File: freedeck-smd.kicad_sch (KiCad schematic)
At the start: 27 parts, among them T1 TP-SM-C-100, T2 TP-SM-C-100, U1 RP2040, U2 W25Q128JV, Y1 ABM8-12.000MHZ-B2-T

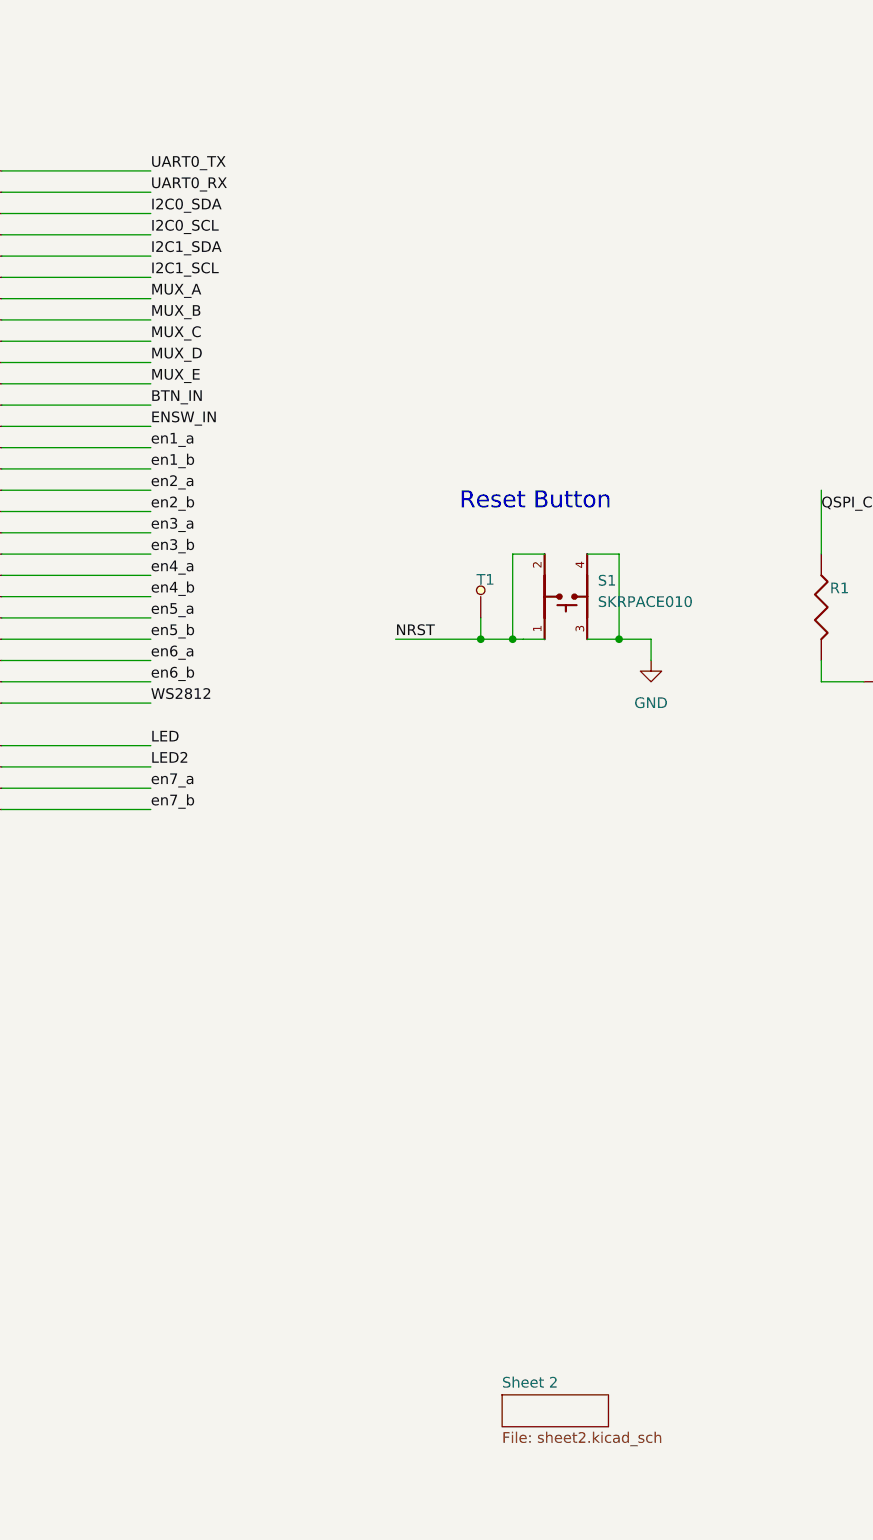
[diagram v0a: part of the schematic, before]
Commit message: Added multiplexers, changed i2c to spi, added external pins
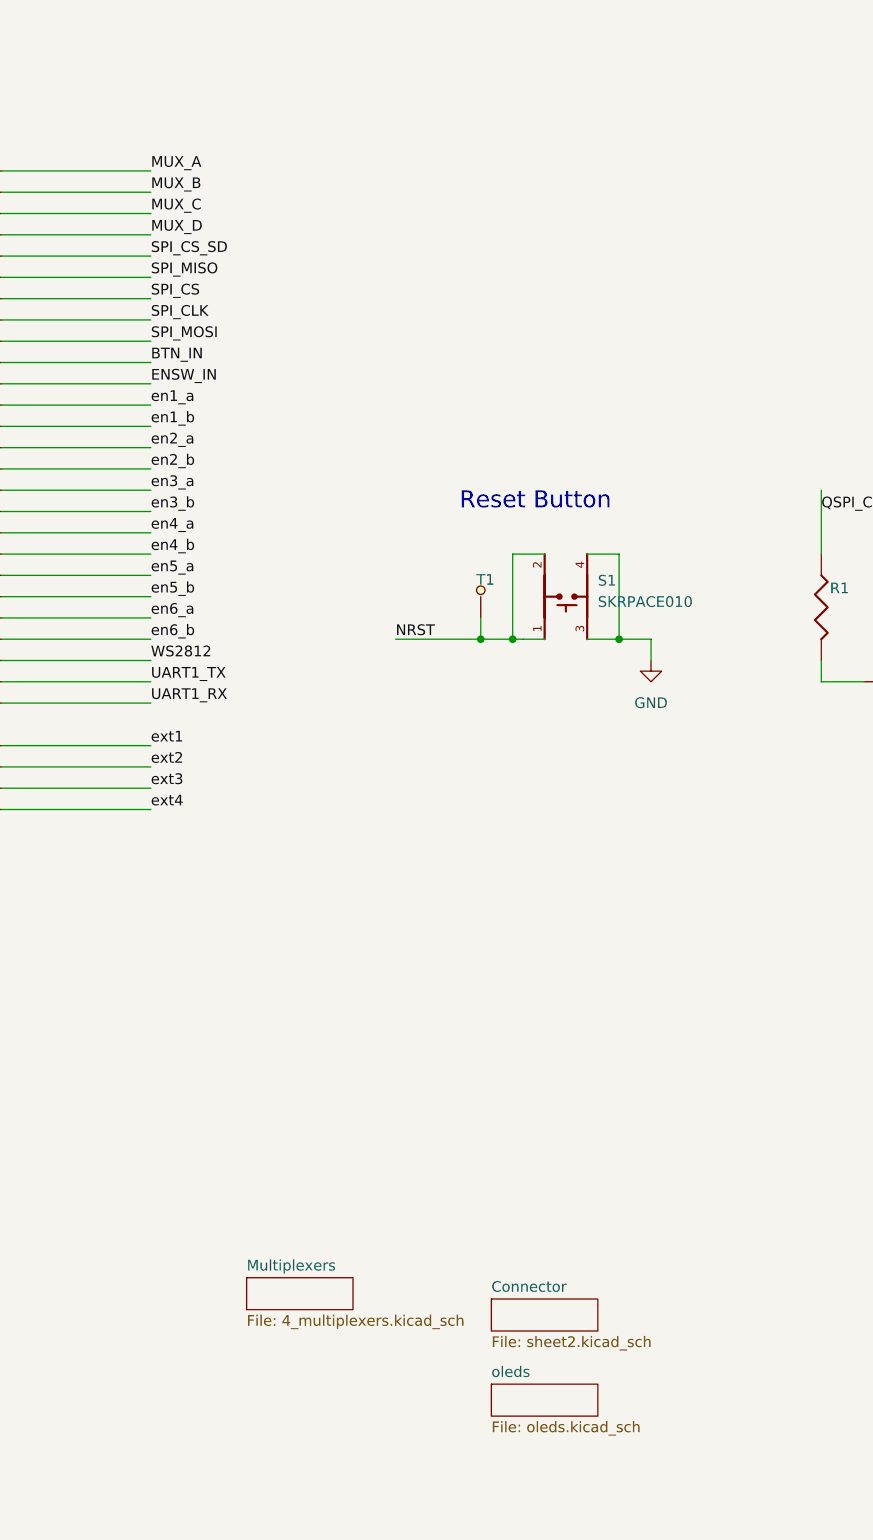
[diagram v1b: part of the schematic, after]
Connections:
- net I2C0_SCL is gone; now on net MUX_D: U1.5 (GPIO3)
- net I2C0_SDA is gone; now on net MUX_C: U1.4 (GPIO2)
- net MUX_E is gone; now on net ENSW_IN: U1.13 (GPIO10)
- net UART0_RX is gone; now on net MUX_B: U1.3 (GPIO1)
- net UART0_TX is gone; now on net MUX_A: U1.2 (GPIO0)
- net BTN_IN: now also U1.12 (GPIO9); no longer U1.14 (GPIO11)
- net ENSW_IN: no longer U1.15 (GPIO12)
- net MUX_A: no longer U1.8 (GPIO6)
- net MUX_B: no longer U1.9 (GPIO7)
- net MUX_C: no longer U1.11 (GPIO8)
- net MUX_D: no longer U1.12 (GPIO9)
- net WS2812: now also U1.35 (GPIO23); no longer U1.37 (GPIO25)
- net en1_a: now also U1.14 (GPIO11); no longer U1.16 (GPIO13)
- net en1_b: now also U1.15 (GPIO12); no longer U1.17 (GPIO14)
- net en2_a: now also U1.16 (GPIO13); no longer U1.18 (GPIO15)
- net en2_b: now also U1.17 (GPIO14); no longer U1.27 (GPIO16)
- net en3_a: now also U1.18 (GPIO15); no longer U1.28 (GPIO17)
- net en3_b: now also U1.27 (GPIO16); no longer U1.29 (GPIO18)
- net en4_a: now also U1.28 (GPIO17); no longer U1.30 (GPIO19)
- net en4_b: now also U1.29 (GPIO18); no longer U1.31 (GPIO20)
- net en5_a: now also U1.30 (GPIO19); no longer U1.32 (GPIO21)
- net en5_b: now also U1.31 (GPIO20); no longer U1.34 (GPIO22)
- net en6_a: now also U1.32 (GPIO21); no longer U1.35 (GPIO23)
- net en6_b: now also U1.34 (GPIO22); no longer U1.36 (GPIO24)
- net I2C1_SCL renamed SPI_MISO
- net I2C1_SDA renamed SPI_CS_SD
- net LED renamed ext1
- net LED2 renamed ext2
- net en7_a renamed ext3
- net en7_b renamed ext4
- new net SPI_CLK: U1.9 (GPIO7)
- new net SPI_CS: U1.8 (GPIO6)
- new net SPI_MOSI: U1.11 (GPIO8)
- new net UART1_RX: U1.37 (GPIO25)
- new net UART1_TX: U1.36 (GPIO24)
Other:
- sheet Sheet 2 renamed Connector
- added sheet Multiplexers (4_multiplexers.kicad_sch)
- added sheet oleds (oleds.kicad_sch)
